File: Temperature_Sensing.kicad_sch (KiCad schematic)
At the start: 30 parts, among them J3 temptap0, J6 Conn_01x05_Pin, J7 temptap1, J8 extratemp1, J9 extratemp2, SW3 SW_DIP_x02, U1 ADS131M08QPBSRQ1

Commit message: nothing changedgit add .git add . (do not look at commit history :))
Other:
- title: (none) -> BPS Voltage&Temperature board 
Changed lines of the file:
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@@
 	(generator_version "8.0")
 	(paper "A4")
+	(title_block
+		(title "BPS Voltage&Temperature board ")
+		(date "2025-03-05")
+	)
 	(junction
 		(at 139.7 63.5)

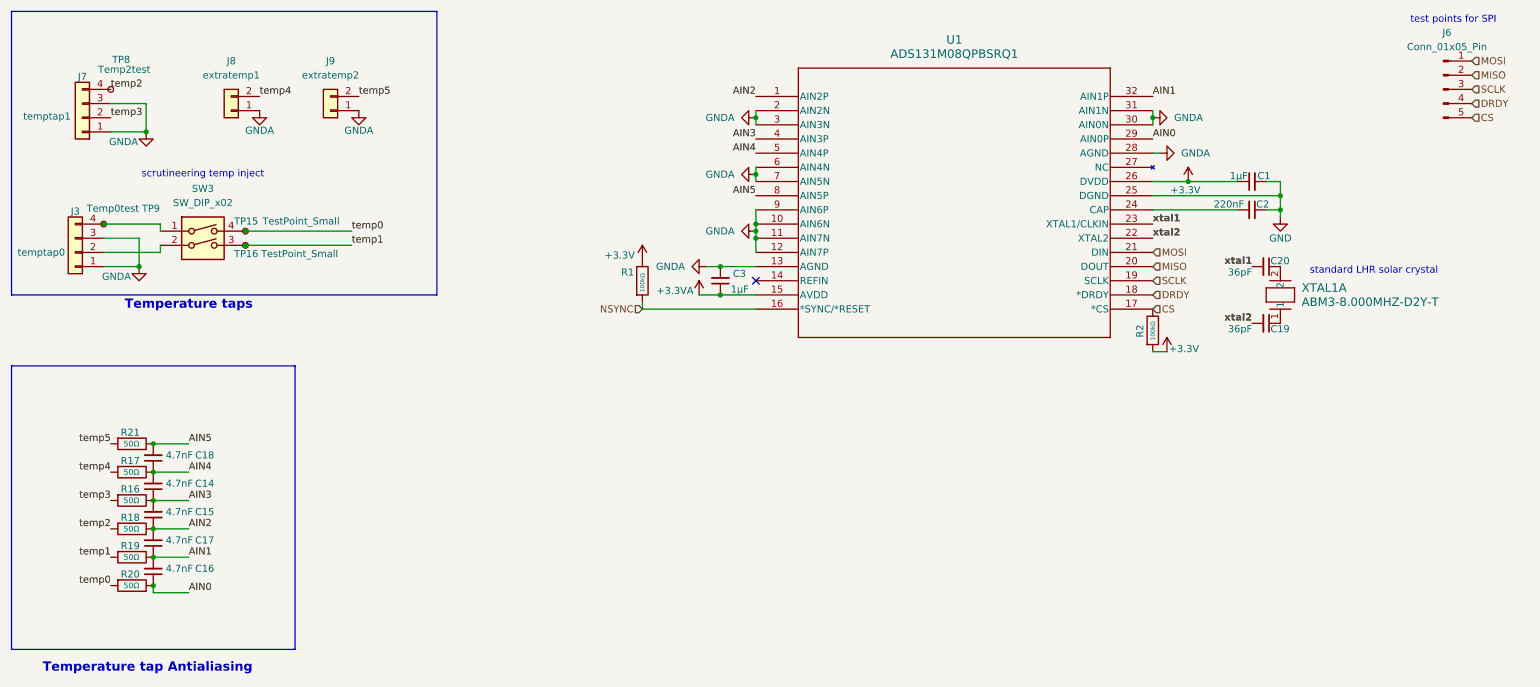
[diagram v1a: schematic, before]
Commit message: concerns from review council addressed
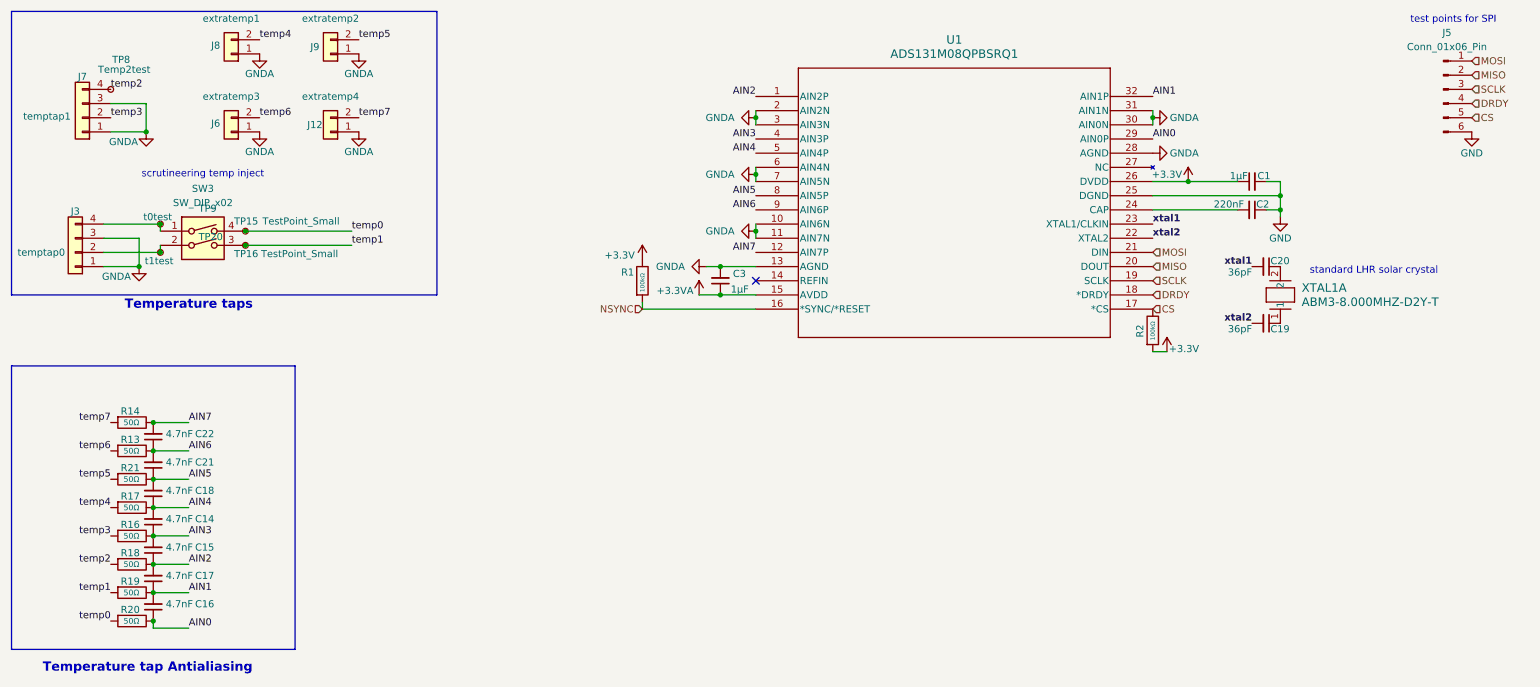
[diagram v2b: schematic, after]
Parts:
- removed J6: Conn_01x05_Pin, symbol Connector:Conn_01x05_Pin
- added C21, C22: 4.7nF, Capacitor_SMD:C_0805_2012Metric, symbol Device:C_Small
- added J12: extratemp4, Connector_Molex:Molex_Nano-Fit_105313-xx02_1x02_P2.50mm_Horizontal, symbol Connector_Generic:Conn_01x02
- added J5: Conn_01x06_Pin, symbol Connector:Conn_01x06_Pin
- added J6: extratemp3, Connector_Molex:Molex_Nano-Fit_105313-xx02_1x02_P2.50mm_Horizontal, symbol Connector_Generic:Conn_01x02
- added R13, R14: 50Ω, Resistor_SMD:R_0805_2012Metric, symbol Device:R
- added TP20: t1test, symbol Connector:TestPoint_Small
- TP9: value Temp0test -> t0test
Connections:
- net AIN5: now also C21.1
- net CS: now also J5.5 (Pin_5)
- net DRDY: now also J5.4 (Pin_4)
- net GND: now also J5.6 (Pin_6)
- net GNDA: now also J12.1 (Pin_1), J6.1 (Pin_1); no longer U1.12 (AIN7P), U1.9 (AIN6P)
- net MISO: now also J5.2 (Pin_2)
- net MOSI: now also J5.1 (Pin_1)
- net SCLK: now also J5.3 (Pin_3)
- net at J3.2 (Pin_2), SW3.2: now also TP20.1
- new net AIN6: C21.2, C22.1, R13.1, U1.9 (AIN6P)
- new net AIN7: C22.2, R14.1, U1.12 (AIN7P)
- new net temp6: J6.2 (Pin_2), R13.2
- new net temp7: J12.2 (Pin_2), R14.2
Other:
- company: (none) -> LHR Solar: Battery Protection System
- moved on the sheet: C14, C15, C16, C17, C18, J8, J9, R16, R17, R18, R19, R20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

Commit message: schematic should be finished. Preliminary layout with changes from review
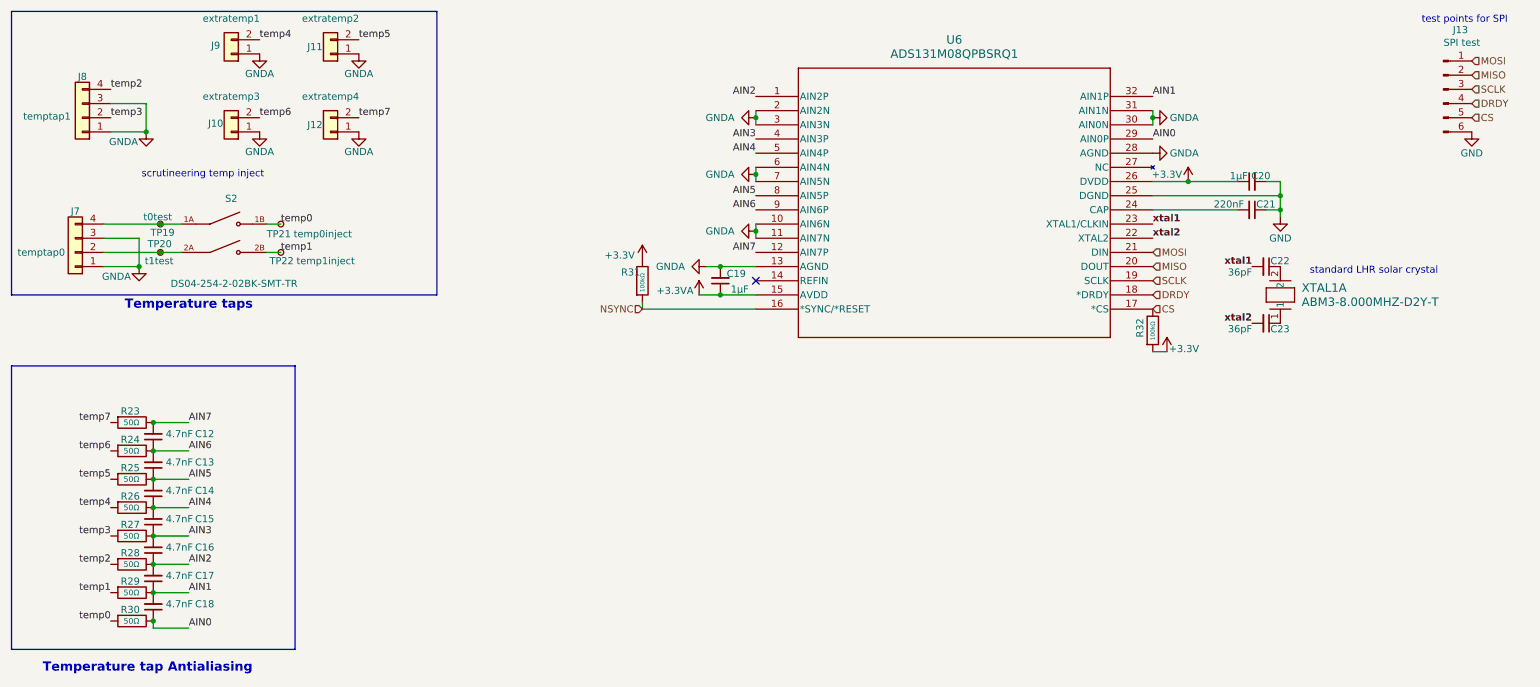
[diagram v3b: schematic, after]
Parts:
- removed SW3: SW_DIP_x02, symbol Switch:SW_DIP_x02
- removed TP15, TP16: TestPoint_Small, symbol Connector:TestPoint_Small
- removed TP8: Temp2test, symbol Connector:TestPoint_Small
- added S2: DS04-254-2-02BK-SMT-TR, footprints:SW_DS04-254-2-02BK-SMT-TR, symbol DS04-254-2-02BK-SMT-TR:DS04-254-2-02BK-SMT-TR
- added TP21: temp0inject, TestPoint:TestPoint_Keystone_5010-5014_Multipurpose, symbol Connector:TestPoint_Small
- added TP22: temp1inject, TestPoint:TestPoint_Keystone_5010-5014_Multipurpose, symbol Connector:TestPoint_Small
- J13: renamed from J5; value Conn_01x06_Pin -> SPI test; footprint (none) -> Connector_PinHeader_2.54mm:PinHeader_1x06_P2.54mm_Vertical
- TP19: renamed from TP9; footprint (none) -> UTSVT_Special:TestPoint_HEX_3mmID
- TP20: footprint (none) -> UTSVT_Special:TestPoint_HEX_3mmID
- renumbered C22 to C12, C21 to C13, C18 to C14, C14 to C15, C15 to C16, C16 to C18, C3 to C19, C1 to C20, C2 to C21, C20 to C22, C19 to C23, J6 to J10, J9 to J11, J3 to J7, J7 to J8, J8 to J9, R14 to R23, R13 to R24, R21 to R25, R17 to R26, R16 to R27, R18 to R28, R19 to R29, R20 to R30, R1 to R31, R2 to R32, U1 to U6
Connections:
- net temp0: now also S2.1B, TP21.1
- net temp1: now also S2.2B, TP22.1
- net at J7.4 (Pin_4), TP19.1: now also S2.1A
- net at J7.2 (Pin_2), TP20.1: now also S2.2A

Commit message: Preliminary schematic done. need to adjust silkscreen and what not
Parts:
- C22, C23: value 36pF -> 18pF
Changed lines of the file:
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@@
 			)
 		)
-		(property "Value" "36pF"
+		(property "Value" "18pF"
 			(at 230.632 69.596 90)
 			(effects
@@
 			)
 		)
-		(property "Value" "36pF"
+		(property "Value" "18pF"
 			(at 230.632 59.436 90)
 			(effects

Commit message: 1st layout done. silkscreen done. BOM added.
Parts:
- C12, C13, C14, C15, C16, C17, C18: P/N (none) -> 80-C0805C472J3GAUTO
- C19, C20: P/N (none) -> C0805C105K5PACTU
- C21: P/N (none) -> 80-C0805C22JCRTU
- C22, C23: P/N (none) -> 581-KGU21RCG2E180FU
- J10, J11, J12, J9: P/N (none) -> 538-105313-2102
- J7, J8: P/N (none) -> 538-105313-2104
- R23, R24, R25, R26, R27, R28, R29, R30: P/N (none) -> 71-CRCW0805-50
- R31, R32: P/N (none) -> CRCW0805100KFKEAC
- S2: P/N (none) -> 490-DS04254202BK-STR
- U6: P/N (none) -> 595-ADS131M08QPBSRQ1
- XTAL1: P/N (none) -> 815-ABM3-8-D2Y-T
